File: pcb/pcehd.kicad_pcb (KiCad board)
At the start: 2 copper layers, 118.2 x 73 mm, 164 parts, among them J1 HDMI_CONN, J2 Micro_SD_Card, P1 JTAG_CONN, Q1 BC847, Q2 BC847, U1 AP7361, U10 SN74LVCC4245APW, U11 SN74LVCC4245APW, U12 10CL025YE144C8N, U13 IS25LP016D-JBLE, U14 SN74LVCC4245APW, U15 TLV70012, U16 TLV70025, U17 TLV70012, U18 SN74LVCC4245APW, U19 SN74LVCC4245APW, U2 ADV7513, U20 SN74LVC2G17, U3 TLV70018, U4 PCEngineExpansion, U5 FS7140-01G-XTD, U6 PCM1808PWR, U7 SI5351C-B, U8 74153, U9 SN74LVCC4245APW, Y1 25.000MHz

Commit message: Layout almost done
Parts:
- C39, C40, C41, C43, C44, C45, C47, C48, C49, C51, C52, C53, C55, C56, C57, C58, C59, C60, C61, C62, C65, R8: moved to B.Cu
- moved R14 145.3 mm to (137.5, 62.9), turned to 225 degrees
- moved C65 133.3 mm to (133.8, 71.2), turned to 0 degrees
- moved C58 131.6 mm to (129.5, 67.4)
- moved C62 127.0 mm to (140.9, 85.5), turned to 270 degrees
- moved C56 125.2 mm to (126.2, 71.6), turned to 180 degrees
- moved C49 117.2 mm to (120.8, 75.4), turned to 270 degrees
- moved C45 117.1 mm to (115.8, 76.4)
- moved C63 111.9 mm to (139.5, 70.2), turned to 45 degrees
- moved C64 111.1 mm to (143.2, 77.2), turned to 135 degrees
- moved C37 109.6 mm to (113.4, 85.7)
- moved C60 108.7 mm to (139.9, 77.7), turned to 135 degrees
- moved C61 107.6 mm to (142.8, 83.7), turned to 270 degrees
- moved C44 106.5 mm to (118.4, 80.5), turned to 270 degrees
- moved C59 104.8 mm to (133.3, 69.1), turned to 270 degrees
- moved C52 103.7 mm to (123.5, 71.6), turned to 0 degrees
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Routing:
- net /fpga1/VCCA: track 82.6 -> 133.2 mm, vias 8 -> 10
- net Net-(R8-Pad1): track 0.00 -> 39.2 mm, vias 0 -> 1
- net Net-(R14-Pad2): track 0.00 -> 25.9 mm, vias 0 -> 2
- net VCC: track 610.5 -> 634.4 mm, vias 34 -> 36
- net GND: track 11.5 -> 29.4 mm, vias 0 -> 2
- net /fpga1/VCCINT: track 126.2 -> 143.4 mm, vias 7 -> 12
- net /fpga1/TMS: track 105.0 -> 89.5 mm
- net /fpga1/TDO: track 91.3 -> 76.4 mm
- net /fpga1/A18: track 54.3 -> 61.4 mm
- net /fpga1/VCCD_PLL: track 77.5 -> 84.1 mm, vias 7 -> 10
- net /fpga1/A14: track 52.3 -> 58.5 mm
- net /fpga1/A17: track 51.2 -> 57.4 mm
- net /fpga1/A9: track 50.2 -> 56.4 mm
- net /fpga1/A8: track 49.1 -> 55.0 mm
- net Net-(JP1-Pad1): track 55.5 -> 57.4 mm
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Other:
- net class Power: trace_width 0.35 -> 0.25

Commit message: 100% parts placed, 95% routed
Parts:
- C35, C36, C38, C50, C54, C66: moved to B.Cu
- moved C66 138.0 mm to (143.7, 73.5)
- moved C67 136.0 mm to (145.4, 73.6), turned to 135 degrees
- moved C69 134.5 mm to (146.6, 72.4), turned to 135 degrees
- moved C54 127.2 mm to (145.0, 86.7), turned to 45 degrees
- moved C50 117.0 mm to (140.7, 94.6), turned to 270 degrees
- moved C36 116.6 mm to (115.8, 81.3)
- moved C38 115.2 mm to (127.8, 93.5), turned to 180 degrees
- moved C35 109.5 mm to (126.0, 97.9), turned to 270 degrees
- moved C61 4.28 mm to (138.7, 82.5), turned to 180 degrees
- moved D3 1.48 mm to (163.1, 91.1)
- moved D2 1.30 mm to (166.6, 91.1)
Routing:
- net GND: track 29.4 -> 749.2 mm, vias 2 -> 109
- net VCC: track 634.4 -> 671.2 mm, vias 36 -> 43
- net /fpga1/VCCA: track 133.2 -> 170.0 mm, vias 10 -> 12
- net /input1/CS: track 0.00 -> 19.9 mm
- net /fpga1/VCCINT: track 143.4 -> 159.8 mm, vias 12 -> 13
- net /fpga1/TMS: track 89.5 -> 100.9 mm
- net /fpga1/TDO: track 76.4 -> 87.4 mm
- net Net-(R26-Pad2): track 68.6 -> 74.6 mm, vias 0 -> 2
- net /hdmitx1/DVDD1V8_FILT_AVDD: track 39.6 -> 44.3 mm
- net /hdmitx1/5V_FUSED: track 17.2 -> 21.4 mm, vias 2 -> 3
- net Net-(R28-Pad2): track 58.0 -> 61.7 mm, vias 0 -> 2
- net Net-(U7-Pad6): track 26.8 -> 30.0 mm
- net /hdmitx1/DVDD1V8_FILT_DVDD: track 48.3 -> 51.2 mm
- net GNDREF: track 11.5 -> 14.0 mm
- net /fpga1/DDIR: track 129.3 -> 131.3 mm
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- added copper zone on B.Cu, net GND
- added copper zone on F.Cu, net GND
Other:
- net class Power: via_dia 1 -> 0.8

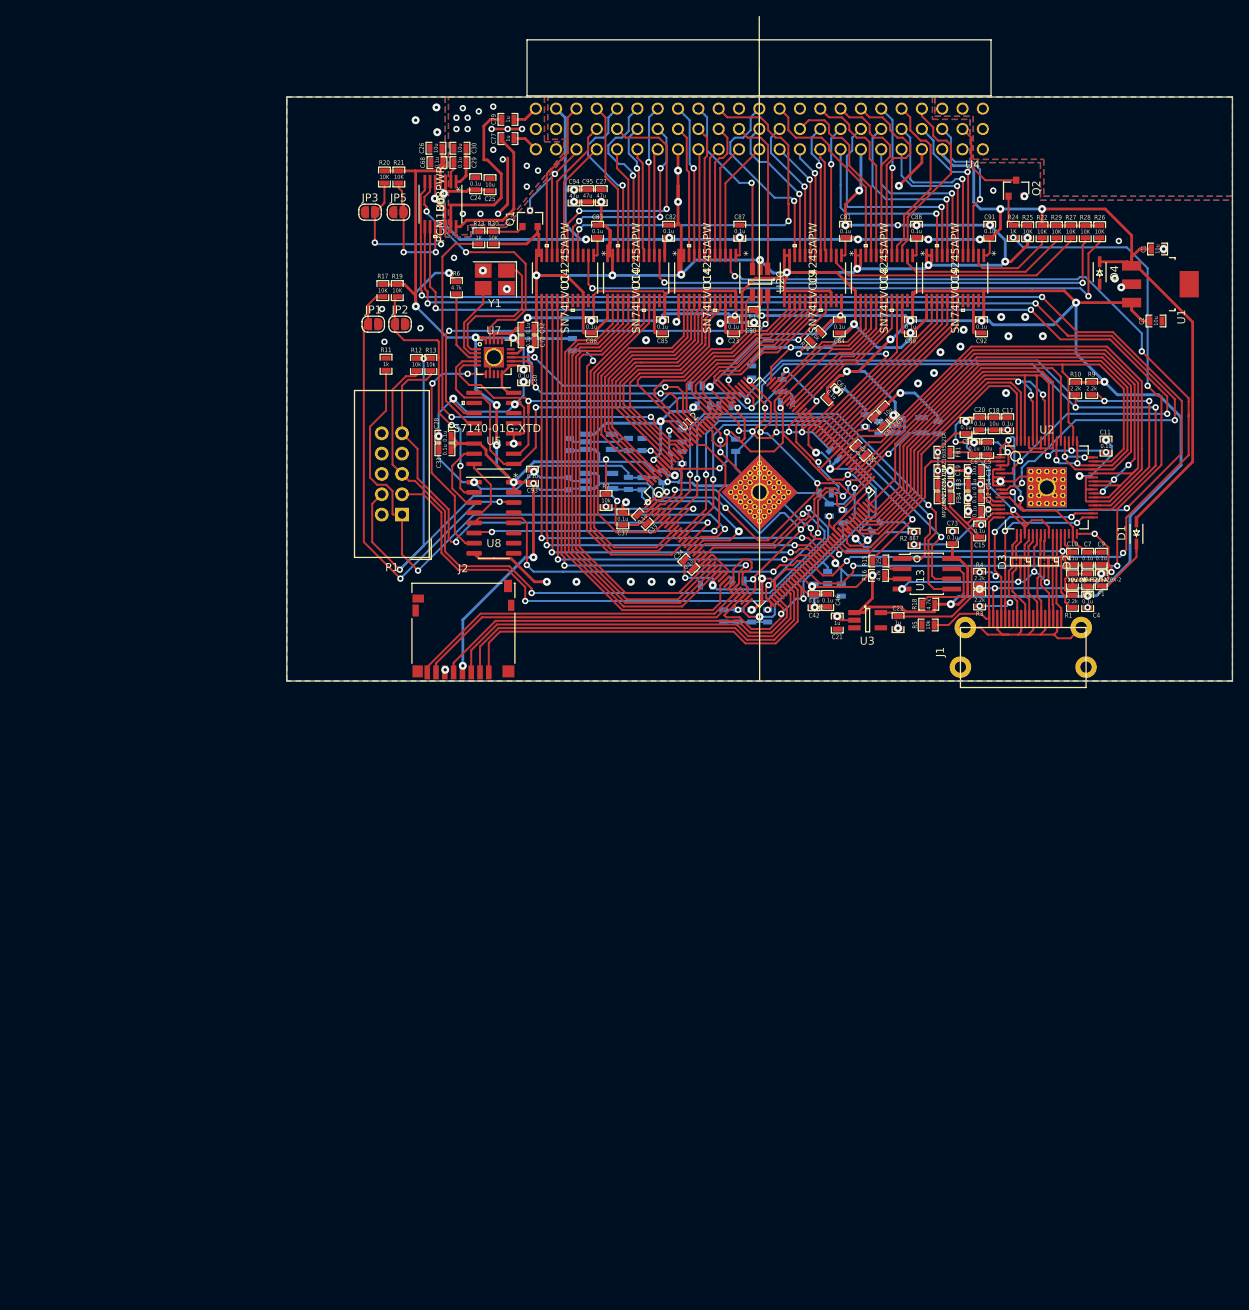
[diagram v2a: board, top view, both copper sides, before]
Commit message: Removed bypass components and routed all power
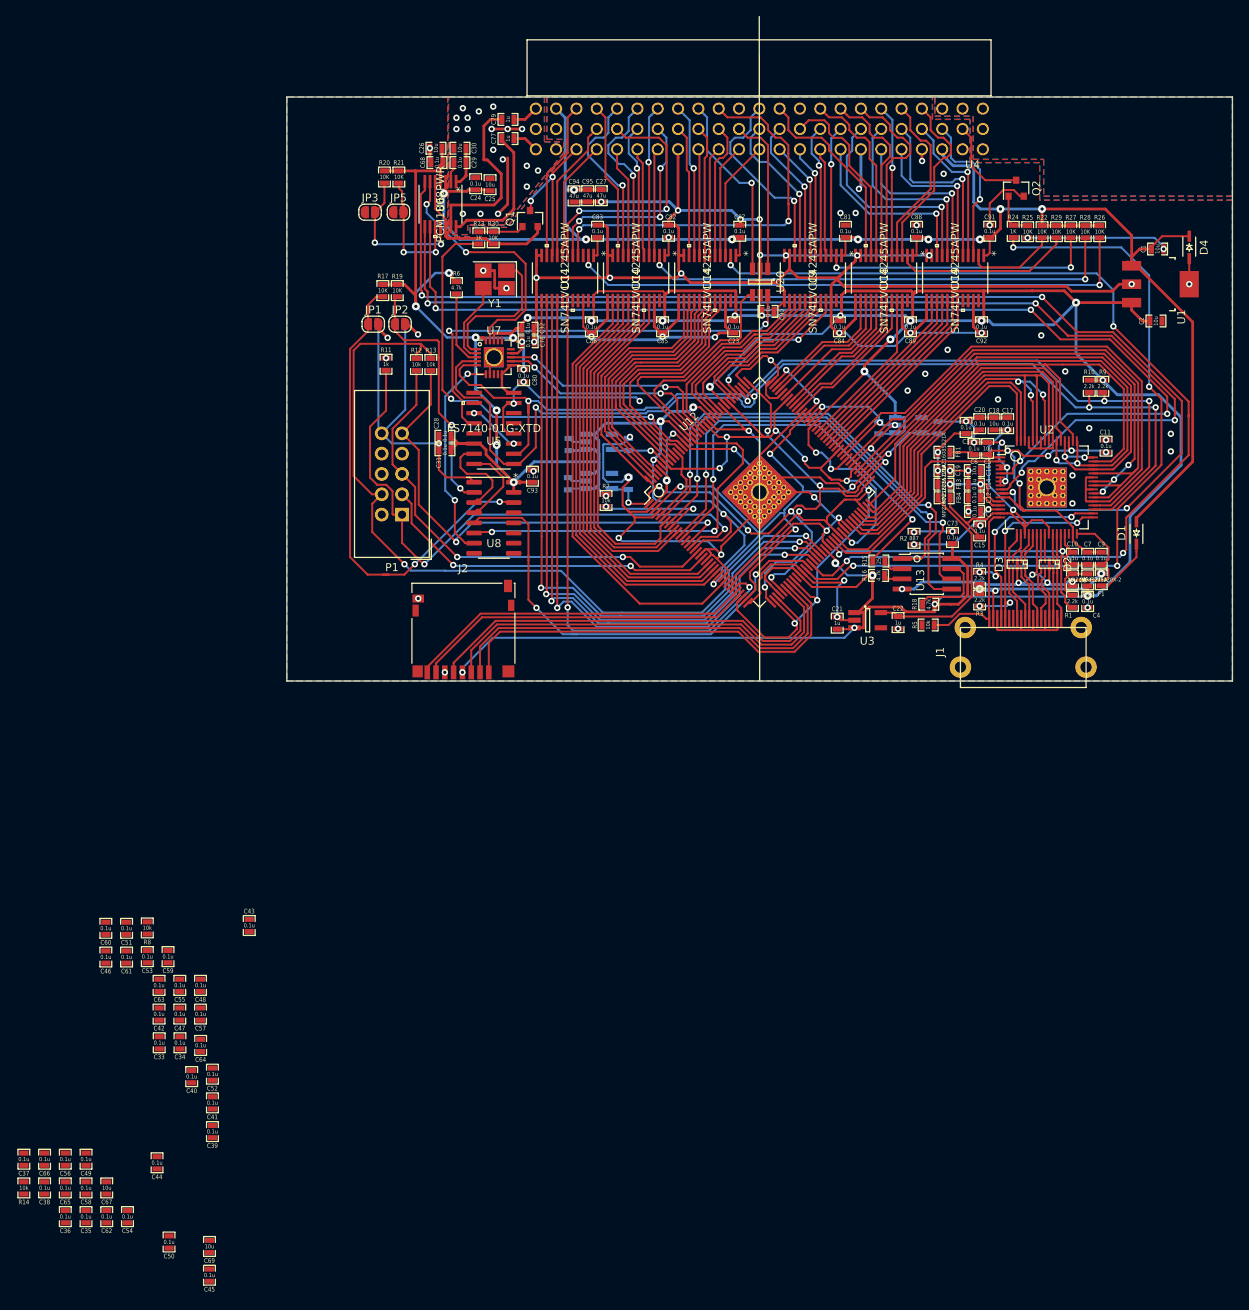
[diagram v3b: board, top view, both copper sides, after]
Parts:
- C35, C36, C38, C39, C40, C41, C43, C44, C45, C47, C48, C49, C50, C51, C52, C53, C54, C55, C56, C57, C58, C59, C60, C61, C62, C65, C66, R8: moved to F.Cu
- moved R14 145.3 mm to (38.5, 169.4), turned to 90 degrees
- moved C66 138.0 mm to (41.1, 165.8)
- moved C67 136.0 mm to (48.9, 169.4), turned to 90 degrees
- moved C69 134.5 mm to (61.7, 176.7), turned to 90 degrees
- moved C65 133.3 mm to (43.7, 169.4), turned to 90 degrees
- moved C58 131.6 mm to (46.3, 169.4)
- moved C54 127.2 mm to (51.5, 173.0), turned to 90 degrees
- moved C62 127.0 mm to (48.9, 173.0), turned to 90 degrees
- moved C56 125.2 mm to (43.7, 165.8), turned to 90 degrees
- moved C49 117.2 mm to (46.3, 165.8), turned to 90 degrees
- moved C45 117.1 mm to (61.7, 180.3)
- moved C50 117.0 mm to (56.7, 176.1), turned to 90 degrees
- moved C36 116.6 mm to (43.7, 173.0)
- moved C38 115.2 mm to (41.1, 169.4), turned to 90 degrees
- moved C63 111.9 mm to (55.4, 144.0), turned to 90 degrees
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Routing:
- net GND: track 749.2 -> 799.7 mm, vias 109 -> 94
- net /fpga1/TDO: track 87.4 -> 43.6 mm
- net /fpga1/TMS: track 100.9 -> 59.1 mm
- net Net-(R8-Pad1): track 39.2 -> 0.00 mm, vias 1 -> 0
- net Net-(R14-Pad2): track 25.9 -> 0.00 mm, vias 2 -> 0
- net /fpga1/VCCINT: track 159.8 -> 142.8 mm, vias 13 -> 10
- net /fpga1/CS: track 65.5 -> 79.0 mm
- net /fpga1/HuID_N: track 65.2 -> 78.3 mm
- net /fpga1/WR_N: track 65.3 -> 78.2 mm
- net /fpga1/CEK: track 64.9 -> 77.5 mm
- net VCC: track 671.2 -> 659.5 mm, vias 43 -> 37
- net /fpga1/VCCA: track 170.0 -> 180.7 mm, vias 12 -> 8
- net /fpga1/DCKFB: track 48.7 -> 59.4 mm
- net /fpga1/XRD: track 59.8 -> 68.9 mm
- net /fpga1/VCCD_PLL: track 85.8 -> 77.9 mm, vias 10 -> 7
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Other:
- net class Power: trace_width 0.25 -> 0.35

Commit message: Finished place and route
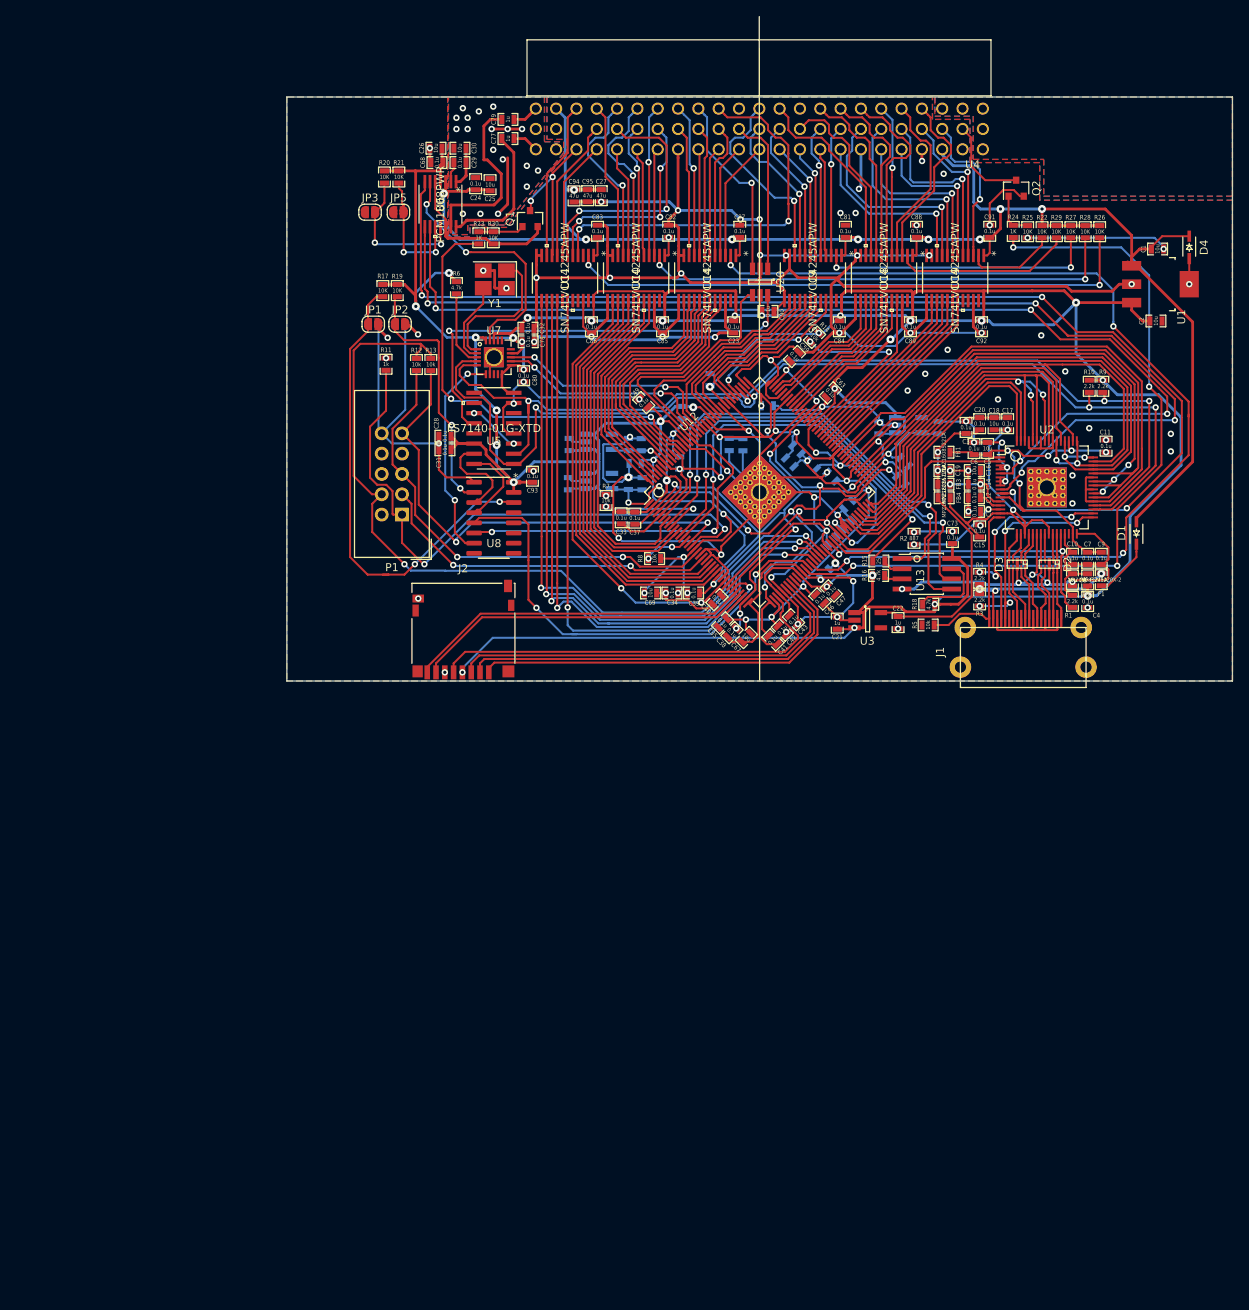
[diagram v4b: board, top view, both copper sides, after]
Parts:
- C36, C44, C45, C48, C50, C51, C52, C53, C54, C55, C56, C57, C58, C60, C61, C62, C64, C65, C66: moved to B.Cu
- moved R14 145.2 mm to (137.4, 63.0), turned to 225 degrees
- moved C62 135.3 mm to (148.2, 81.0), turned to 315 degrees
- moved C58 129.7 mm to (131.5, 71.6), turned to 0 degrees
- moved C66 129.3 mm to (135.2, 77.1), turned to 315 degrees
- moved C65 128.2 mm to (134.3, 78.7), turned to 315 degrees
- moved C54 124.9 mm to (141.5, 86.5), turned to 45 degrees
- moved C56 123.1 mm to (128.4, 76.5), turned to 270 degrees
- moved C49 117.5 mm to (116.0, 71.2), turned to 135 degrees
- moved C50 117.1 mm to (138.7, 92.5), turned to 225 degrees
- moved C45 117.0 mm to (115.7, 76.5)
- moved C36 116.6 mm to (115.8, 81.3)
- moved C61 115.3 mm to (148.6, 78.6), turned to 315 degrees
- moved C63 111.9 mm to (139.3, 70.0), turned to 225 degrees
- moved C37 110.7 mm to (114.9, 85.6)
- moved C38 110.5 mm to (127.0, 100.0), turned to 225 degrees
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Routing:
- net GND: track 799.7 -> 914.6 mm, vias 94 -> 101
- net VCC: track 659.5 -> 694.4 mm, vias 37 -> 43
- net Net-(R14-Pad2): track 0.00 -> 23.2 mm, vias 0 -> 2
- net /fpga1/VCCINT: track 142.8 -> 165.5 mm, vias 10 -> 13
- net /fpga1/VCCD_PLL: track 77.9 -> 91.8 mm, vias 7 -> 9
- net /fpga1/VCCA: track 180.7 -> 191.2 mm, vias 8 -> 10
- net Net-(R8-Pad1): track 0.00 -> 5.75 mm, vias 0 -> 2
- net /fpga1/DAT2: track 54.0 -> 51.2 mm
- net /fpga1/DAT3: track 53.9 -> 51.7 mm
- net /fpga1/DCK: track 80.1 -> 78.0 mm
- net /fpga1/CMD: track 53.8 -> 51.8 mm
- net /fpga1/SCLK: track 53.7 -> 52.0 mm
- net /fpga1/G1: track 66.5 -> 67.3 mm
- net /fpga1/DDIR: track 131.6 -> 131.0 mm
- net /fpga1/A18: track 55.4 -> 55.5 mm, vias 0 -> 2
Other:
- net class Power: trace_width 0.35 -> 0.25

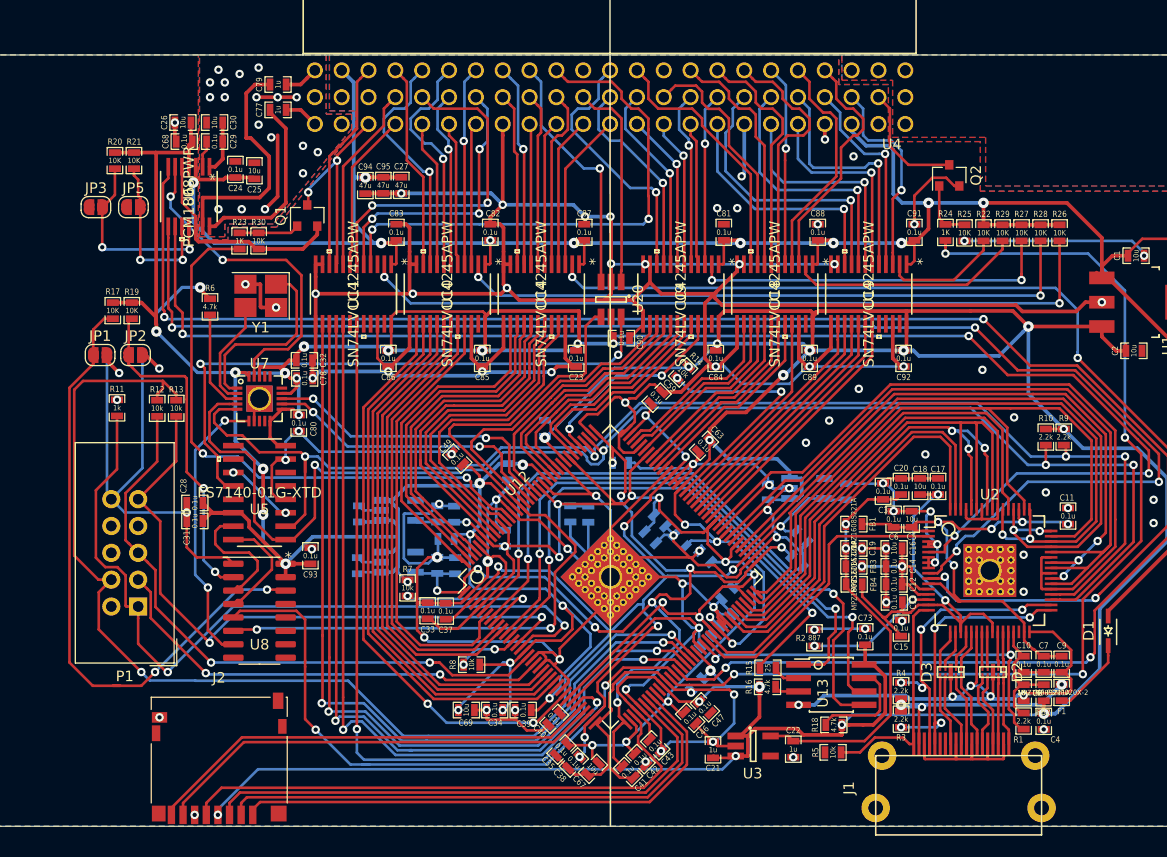
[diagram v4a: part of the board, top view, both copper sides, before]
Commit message: Added CDD signal to last open IO pin
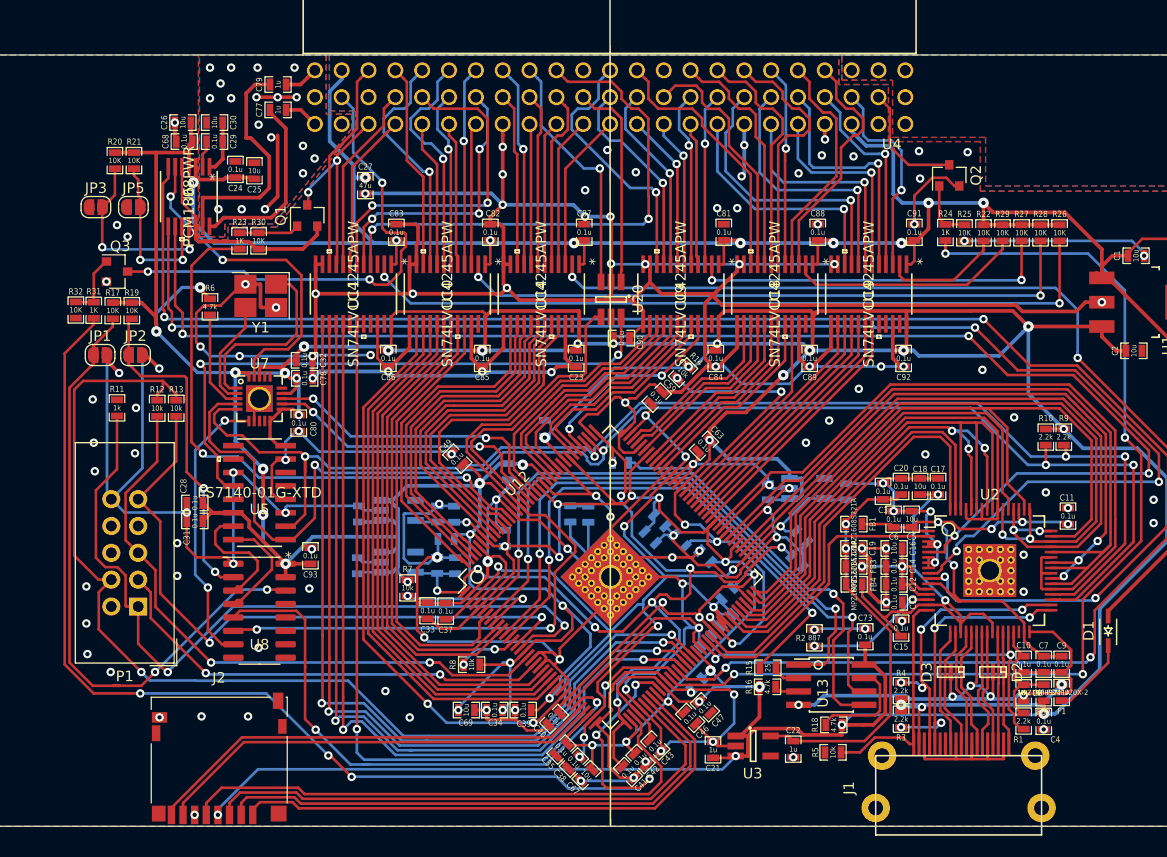
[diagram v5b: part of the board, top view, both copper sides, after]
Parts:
- removed C94, C95: 47u, custom_components:SM0603_Capa_libcms
- added Q3: BC847, Package_TO_SOT_SMD:SOT-23, F.Cu at (83.8, 53.5)
- added R31: 1K, custom_components:SM0603_Resistor_libcms, F.Cu at (81.6, 57.2)
- added R32: 10K, custom_components:SM0603_Resistor_libcms, F.Cu at (79.9, 57.1)
- moved C27 3.40 mm to (107.3, 45.4)
- moved C67 0.85 mm to (128.2, 101.2)
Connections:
- U12 pad 46: (no net) -> /input1/CDD_I
- U4 pad B2: (no net) -> /input1/CDD
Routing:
- net /input1/CDD_I: track 0.00 -> 113.3 mm, vias 0 -> 6
- net GND: track 914.6 -> 967.3 mm, vias 101 -> 141
- net /input1/CDD: track 0.00 -> 47.1 mm, vias 0 -> 3
- net VCC: track 694.4 -> 677.5 mm
- net Net-(Q3-Pad1): track 0.00 -> 6.09 mm
- net /5V: track 222.9 -> 218.7 mm
- net /fpga1/DCK: track 78.0 -> 75.1 mm
- net /fpga1/DAT3: track 51.7 -> 53.4 mm
- net /fpga1/CMD: track 51.8 -> 53.6 mm
- net /fpga1/DAT2: track 51.2 -> 52.9 mm
- net /fpga1/SCLK: track 52.0 -> 53.1 mm
- net /hdmitx1/TXC-: track 10.5 -> 11.4 mm
- net /hdmitx1/TXC+: track 10.8 -> 11.7 mm
- net /hdmitx1/TX2-: track 9.76 -> 10.7 mm
- net /hdmitx1/TX2+: track 9.94 -> 10.8 mm
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
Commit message: Finished version 0.1
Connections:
- net /input2/HSn renamed /input1/HSn_O
